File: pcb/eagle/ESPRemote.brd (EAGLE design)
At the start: 80 x 20 mm, 29 parts, among them IC1 NCP1117/REG1117, X1 JST-XH-06-PIN-ROUND-PAD

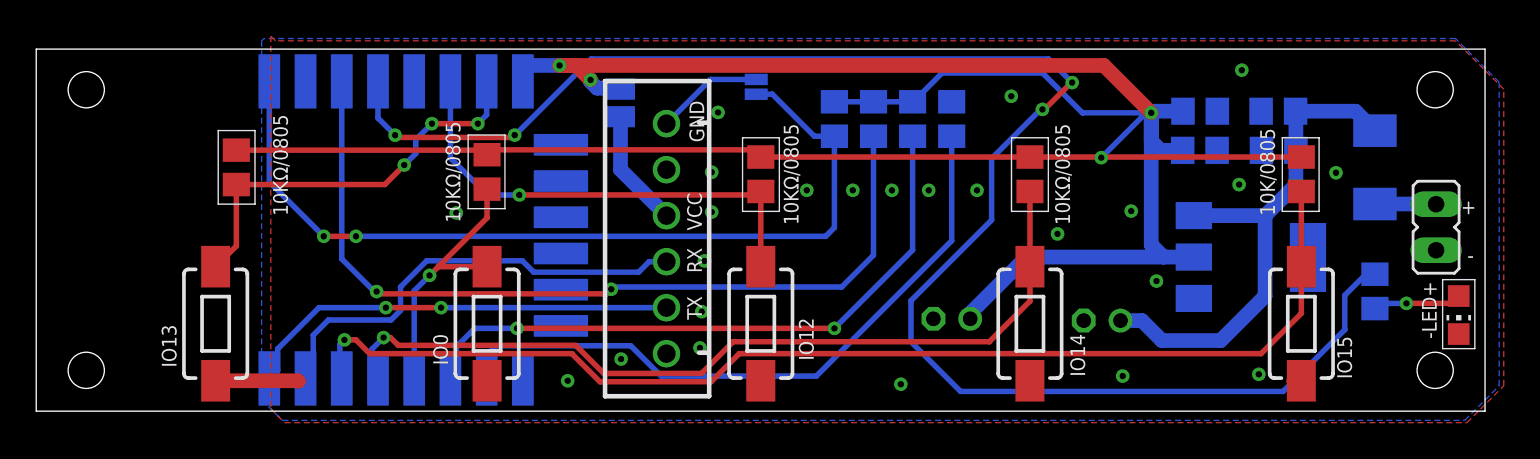
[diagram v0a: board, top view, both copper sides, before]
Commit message: Fix airwires
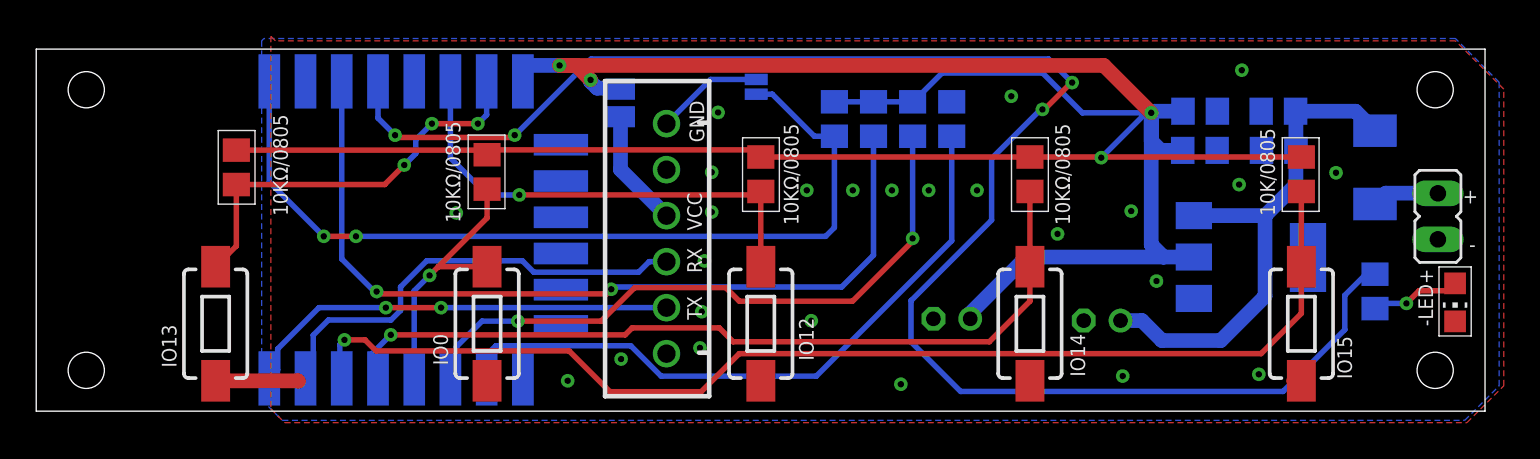
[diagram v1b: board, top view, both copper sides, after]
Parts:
- moved D1 0.73 mm to (78.3, 6.01)
- moved JP2 0.61 mm to (77.4, 10.8)
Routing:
- net GPIO4: track 46.9 -> 45.7 mm
- net GND: vias 24 -> 25
